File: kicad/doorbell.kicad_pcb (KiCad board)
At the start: 4 copper layers, 64 x 59 mm, 77 parts, among them J1 USB-C (USB4105), J2 WF26 bus, K1 GAQW212GS, K2 GAQY212GS, K3 GAQY412EH, K4 GAQY412EH, K5 G6K-2F-Y DC12, Q3 2N7002DW-7-F, SW1 BOOT, SW2 EN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

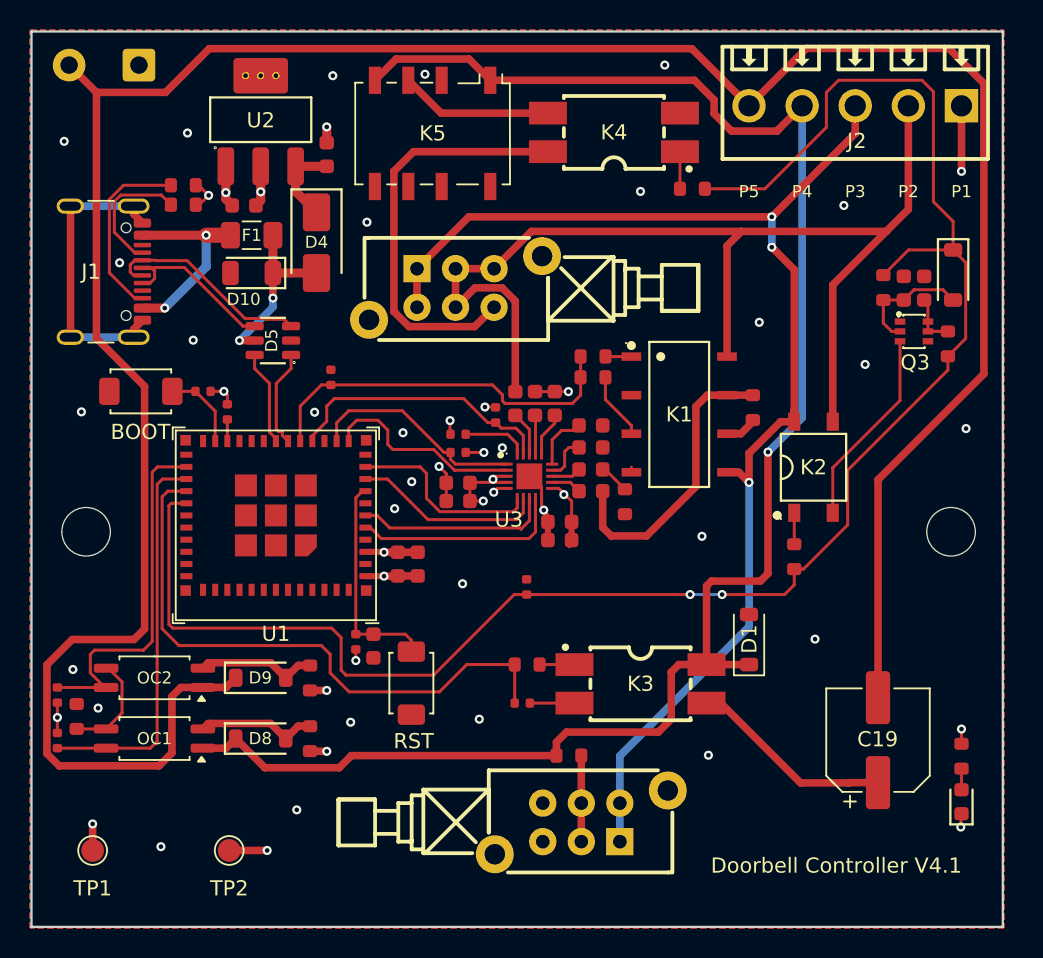
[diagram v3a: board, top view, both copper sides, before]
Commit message: Bus ESD protection placed; sim bidirectional-TVS model + coverage gate
Schematic / PCB:
- Place 4x H24VND3BA bidirectional TVS (D2/D3/D7/D12) clamping P2-P5 -> P1
- Gong cap C19 -> non-polar anti-series pair (C19+C21, 2x 47uF/50V);
  part C3349 (Honor Elec, Economy-PCBA eligible); board re-routed, DRC clean
- R29 -> PCM_JLCPCB-Resistors symbol (was generic Device:R)
- Keep the hard P1<->GND merge; 0R (C17888) / 1M (C17927) breakable bond
  documented as the respin-free alternative

sim:
- Model bidirectional TVS as anti-series Zeners with a standoff (vbr) so it is
  open across the bus range -- fixes the bus being pinned to ~0.8 V
- Add model-coverage gate: every active part must match an explicit reviewed
  model, failing loudly instead of silently using a heuristic fallback

build.sh: pinpoint route.py unrouted connections via the DRC report

docs: TODO / DESIGN / sim README brought in sync with the above
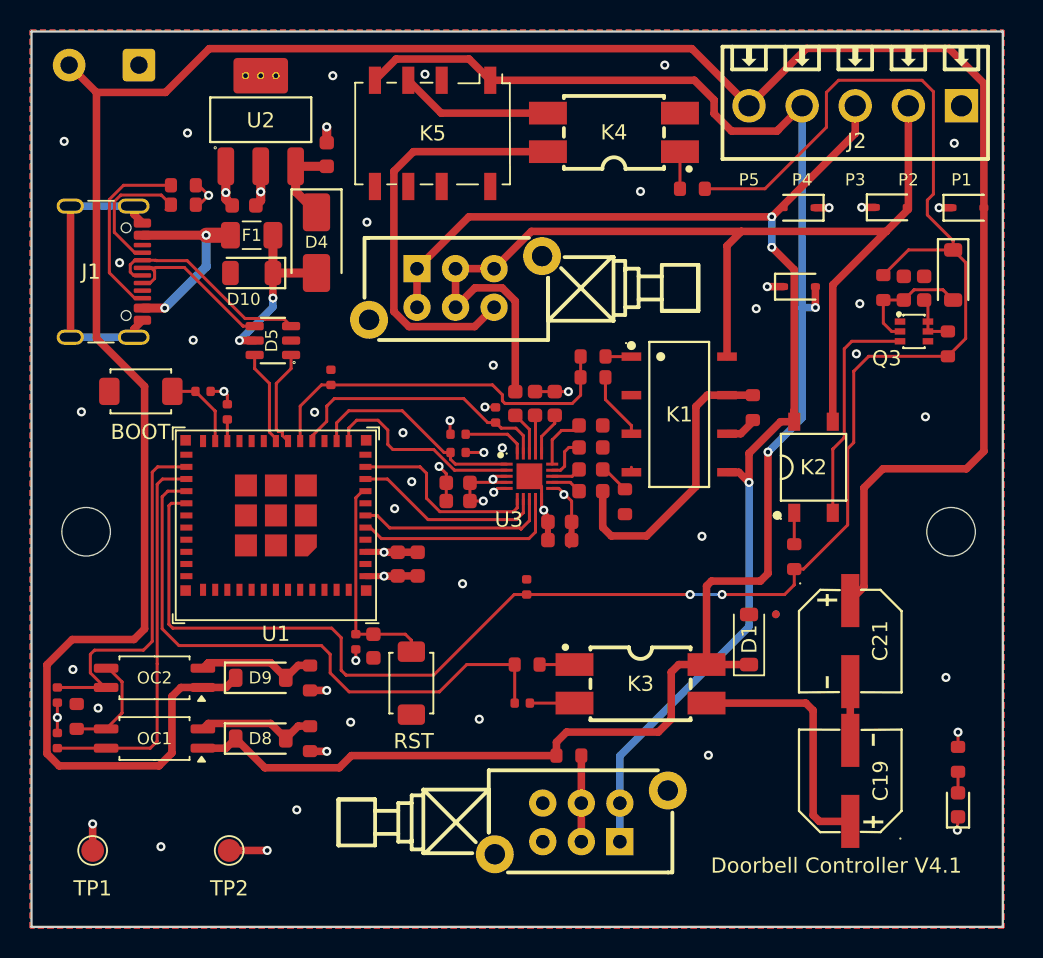
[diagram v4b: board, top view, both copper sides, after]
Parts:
- added C21: 27uF/50V, rvt1h470m0607:CAP-SMD_BD6.3-L6.6-W6.6-LS7.6-FD, F.Cu at (70.4, 56.5)
- added D12: H24VND3BA, PCM_JLCPCB:D_SOD-323, F.Cu at (78.2, 27.9)
- added D2: H24VND3BA, PCM_JLCPCB:D_SOD-323, F.Cu at (73.1, 27.9)
- added D3: H24VND3BA, PCM_JLCPCB:D_SOD-323, F.Cu at (67.0, 27.9)
- added D7: H24VND3BA, PCM_JLCPCB:D_SOD-323, F.Cu at (67.1, 33.1)
- C19: value 22uF/50V -> 27uF/50V; footprint Capacitor_SMD:CP_Elec_6.3x5.4 -> rvt1h470m0607:CAP-SMD_BD6.3-L6.6-W6.6-LS7.6-FD
- moved C19 3.25 mm to (70.4, 65.7)
- moved D6 0.31 mm to (77.5, 67.2)
- moved R15 0.31 mm to (77.5, 64.2)
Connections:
- C19 pad 2: /P5 -> /CHIME_MID
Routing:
- net /CHIME_MID: track 0.00 -> 3.87 mm
- net /DOOR_DRV: track 118.7 -> 122.1 mm
- net /CHIME_C1: track 13.5 -> 16.7 mm
- net /P5: track 177.0 -> 174.5 mm
- net /P4: track 115.6 -> 117.8 mm, vias 1 -> 2
- net /K2_CATH: track 13.2 -> 15.0 mm
- net GND: track 52.2 -> 52.8 mm, vias 43 -> 48

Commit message: Add JLCPCB tooling holes (H3–H5) + STEP fit-test export
- H3–H5: 1.152 mm NPTH JLCPCB tooling holes (PCM_JLCPCB footprint),
  asymmetric. Marked exclude-from-BOM (in_bom no) + exclude_from_pos_files/
  bom on the footprints, like H1/H2, so the BOM/CPL don't demand an LCSC #.
- DRC: exclude the footprint keepout's self-pad false positives (plus the
  attendant silk-over-copper and the floating-thieving isolated-copper
  warnings) → 0 active violations.
- build.sh: new `step` target (also run by all-route) exports
  kicad/fab/doorbell.step. Footprints carrying a truthy custom field
  STEP_Exclude are dropped via kicad/step_exclude.py (kicad-cli's
  --component-filter is include-only, so it emits the complement); SW3/SW4
  flagged so the bare board can be fit-tested against the real switches.
- DESIGN.md: document the tooling holes and the STEP / STEP_Exclude convention.
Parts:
- added H3: ~, PCM_JLCPCB:Hole_Tooling_JLCPCB, F.Cu at (24.8, 72.3)
- added H4: ~, PCM_JLCPCB:Hole_Tooling_JLCPCB, F.Cu at (23.1, 24.1)
- added H5: ~, PCM_JLCPCB:Hole_Tooling_JLCPCB, F.Cu at (78.2, 56.9)
- added Q4: 2N7002, Package_TO_SOT_SMD:SOT-23, F.Cu at (72.2, 36.9)
- C19, C21: value 27uF/50V -> 47uF/50V
- Q3: value 2N7002DW-7-F -> 2N7002; footprint mosfet_2n7002dw:SOT-363_L2.0-W1.3-P0.65-LS2.1-TL -> Package_TO_SOT_SMD:SOT-23
- moved Q3 5.53 mm to (72.1, 41.0), turned to -90 degrees
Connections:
- Q3 pad 1: GND -> /DELAY_GATE
- Q3 pad 2: /WD_GATE -> GND
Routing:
- net /K2_CATH: track 15.0 -> 7.28 mm
- net /DELAY_GATE: track 3.49 -> 10.2 mm
- net /DOOR_DRV: track 122.1 -> 121.4 mm
- net /WD_GATE: track 8.01 -> 7.40 mm
- net GND: vias 48 -> 46

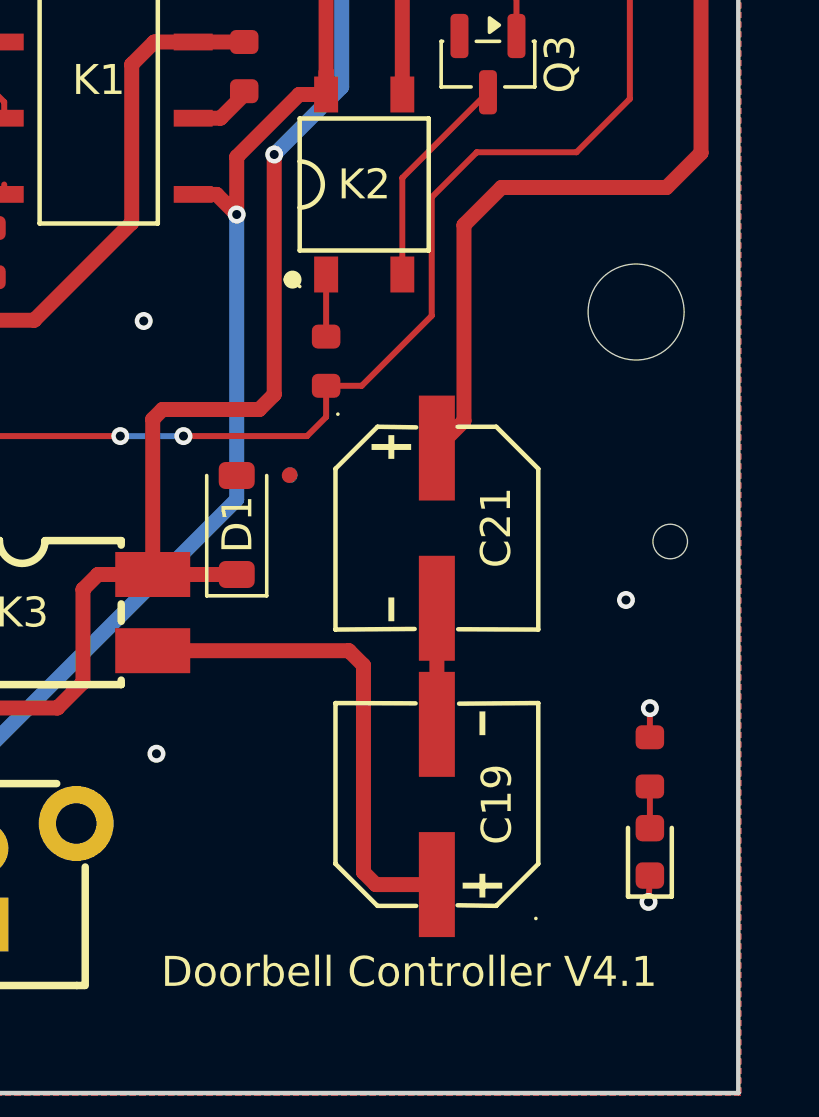
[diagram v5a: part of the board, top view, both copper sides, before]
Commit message: Fix audio/door net descriptions; correct J2 keying note; add fit-test step
Schematic Description fields (kicad/doorbell.kicad_sch):
- C18, D11: were verbatim copy-pastes of C14/D8; corrected to the
  door-lead make-delay cap (R17·C18) and door-watchdog re-arm diode
  (R25·C20·D11) they actually are, per the netlist.
- C14, R28, K1: dropped the stale "K1 gates ->P4" claim — K1 switches
  P2/P3 (the talk handshake via R28), never P4.

Docs:
- TODO/DESIGN/REQUIREMENTS: J2 is a fixed screw terminal (DB125-3.5-5P,
  no plug) — keying is N/A; SAFE-2 survive-miswire rests on the
  bidirectional front-end + non-polar C19 + silkscreen labels.
- ORDERING: added a pre-fab 3D-print fit-test gate (board/enclosure
  fit, connector access, SW3/SW4 actuation — MECH-1/1a).

Verified with ./build.sh all-route: ERC/DRC clean, sim 46/46, fab + STEP
re-exported. Zone fills refreshed on save.
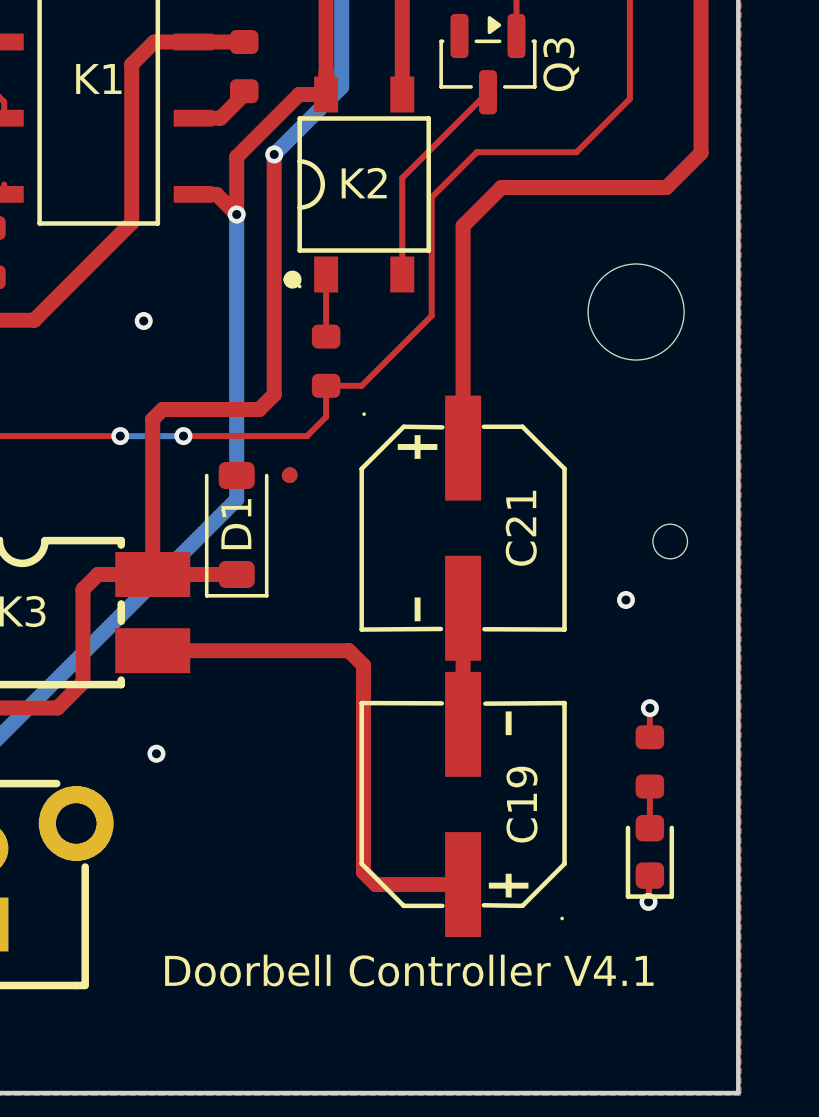
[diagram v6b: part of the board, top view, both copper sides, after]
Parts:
- moved C19 0.88 mm to (71.3, 65.7)
- moved C21 0.88 mm to (71.3, 56.5)
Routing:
- net /CHIME_C1: track 16.7 -> 17.6 mm
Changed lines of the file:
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@@
 		(layer "F.Cu")
 		(at 52.7 68.4)
-		(property "STEP_Exclude" "true"
-			(at 0 0 0)
-			(unlocked yes)
-			(layer "F.Fab")
-			(hide yes)
-			(effects
-				(font
-					(size 1 1)
-					(thickness 0.15)
-				)
-			)
-		)
 		(property "Reference" "SW4"
 			(at 0.05 4.51 0)
@@
 			)
 		)
+		(property "STEP_Exclude" "true"
+			(at 0 0 0)
+			(unlocked yes)
+			(layer "F.Fab")
+			(hide yes)
+			(effects
+				(font
+					(size 1 1)
+					(thickness 0.15)
+				)
+			)
+		)
 		(property "LCSC Part" "C398940"
 			(at 0 0 0)
@@
 	(footprint "rvt1h470m0607:CAP-SMD_BD6.3-L6.6-W6.6-LS7.6-FD"
 		(layer "F.Cu")
-		(at 70.421786 65.665474 90)
+		(at 71.296786 65.665474 90)
 		(descr "47uF 50V ±20%")
 		(property "Reference" "C19"
@@
 		(layer "F.Cu")
 		(at 44.4125 33.185 180)
-		(property "STEP_Exclude" "true"
-			(at 0 0 0)
-			(unlocked yes)
-			(layer "F.Fab")
-			(hide yes)
-			(effects
-				(font
-					(size 1 1)
-					(thickness 0.15)
-				)
-			)
-		)
 		(property "Reference" "SW3"
 			(at -0.0275 -4.765 0)
@@
 			)
 		)
+		(property "STEP_Exclude" "true"
+			(at 0 0 0)
+			(unlocked yes)
+			(layer "F.Fab")
+			(hide yes)
+			(effects
+				(font
+					(size 1 1)
+					(thickness 0.15)
+				)
+			)
+		)
 		(property "LCSC Part" "C398940"
 			(at 0 0 0)
@@
 	(footprint "rvt1h470m0607:CAP-SMD_BD6.3-L6.6-W6.6-LS7.6-FD"
 		(layer "F.Cu")
-		(at 70.421786 56.455474 -90)
+		(at 71.296786 56.455474 -90)
 		(descr "47uF 50V ±20%")
 		(property "Reference" "C21"
@@
 	)
 	(segment
+		(start 79.227 19.708)
+		(end 79.227 43.948)
+		(width 0.5)
+		(layer "F.Cu")
+		(net "/P5")
+	)
+	(segment
 		(start 17.488 58.012)
 		(end 19.15 56.35)
@@
 	)
 	(segment
-		(start 71.325 46.35)
-		(end 71.325 52.88226)
+		(start 67.535 17.4)
+		(end 76.919 17.4)
 		(width 0.5)
 		(layer "F.Cu")
@@
 	)
 	(segment
-		(start 76.919 17.4)
-		(end 79.227 19.708)
+		(start 78.075 45.1)
+		(end 72.575 45.1)
 		(width 0.5)
 		(layer "F.Cu")
@@
 	)
 	(segment
-		(start 67.535 17.4)
-		(end 76.919 17.4)
-		(width 0.5)
-		(layer "F.Cu")
-		(net "/P5")
-	)
-	(segment
 		(start 19.15 56.35)
 		(end 23.225 56.35)
@@
 	)
 	(segment
-		(start 20.75 20.3)
-		(end 25.3 20.3)
-		(width 0.5)
-		(layer "F.Cu")
-		(net "/P5")
-	)
-	(segment
-		(start 27.7625 59.51)
-		(end 26.315 59.51)
-		(width 0.5)
-		(layer "F.Cu")
-		(net "/P5")
-	)
-	(segment
-		(start 78.075 45.1)
-		(end 72.575 45.1)
+		(start 63.75 21.185)
+		(end 67.535 17.4)
 		(width 0.5)
 		(layer "F.Cu")
@@
 	)
 	(segment
-		(start 29.290001 59.51)
-		(end 27.7625 59.51)
+		(start 72.575 45.1)
+		(end 71.296786 46.378214)
 		(width 0.5)
 		(layer "F.Cu")
@@
 	)
 	(segment
-		(start 71.325 52.88226)
-		(end 70.421786 53.785474)
+		(start 20.75 20.3)
+		(end 25.3 20.3)
 		(width 0.5)
 		(layer "F.Cu")
@@
 	)
 	(segment
-		(start 72.575 45.1)
-		(end 71.325 46.35)
+		(start 27.7625 59.51)
+		(end 26.315 59.51)
 		(width 0.5)
 		(layer "F.Cu")
@@
 	)
 	(segment
-		(start 63.75 21.185)
-		(end 67.535 17.4)
+		(start 29.290001 59.51)
+		(end 27.7625 59.51)
 		(width 0.5)
 		(layer "F.Cu")
@@
 	)
 	(segment
-		(start 79.227 19.708)
-		(end 79.227 43.948)
+		(start 63.75 21.185)
+		(end 59.981803 17.416803)
 		(width 0.5)
 		(layer "F.Cu")
@@
 	)
 	(segment
-		(start 63.75 21.185)
-		(end 59.981803 17.416803)
+		(start 76.919 17.4)
+		(end 79.227 19.708)
 		(width 0.5)
 		(layer "F.Cu")
@@
 	)
 	(segment
+		(start 71.296786 46.378214)
+		(end 71.296786 53.785474)
+		(width 0.5)
+		(layer "F.Cu")
+		(net "/P5")
+	)
+	(segment
 		(start 25.725 60.1)
 		(end 25.725 63.825)
@@
 	)
 	(segment
-		(start 60.95 60.54)
-		(end 67.49 60.54)
+		(start 67.49 60.54)
+		(end 67.975 61.025)
 		(width 0.5)
 		(layer "F.Cu")
@@
 	)
 	(segment
-		(start 67.975 61.025)
-		(end 67.975 67.925)
+		(start 67.975 67.925)
+		(end 68.385474 68.335474)
 		(width 0.5)
 		(layer "F.Cu")
@@
 	)
 	(segment
-		(start 67.49 60.54)
-		(end 67.975 61.025)
+		(start 67.975 61.025)
+		(end 67.975 67.925)
 		(width 0.5)
 		(layer "F.Cu")
@@
 	)
 	(segment
-		(start 68.385474 68.335474)
-		(end 70.421786 68.335474)
+		(start 60.95 60.54)
+		(end 67.49 60.54)
 		(width 0.5)
 		(layer "F.Cu")
@@
 	)
 	(segment
-		(start 67.975 67.925)
-		(end 68.385474 68.335474)
+		(start 68.385474 68.335474)
+		(end 71.296786 68.335474)
 		(width 0.5)
 		(layer "F.Cu")
@@
 	)
 	(segment
-		(start 70.421786 62.995474)
-		(end 70.421786 59.125474)
+		(start 71.296786 62.995474)
+		(end 71.296786 59.125474)
 		(width 0.5)
 		(layer "F.Cu")

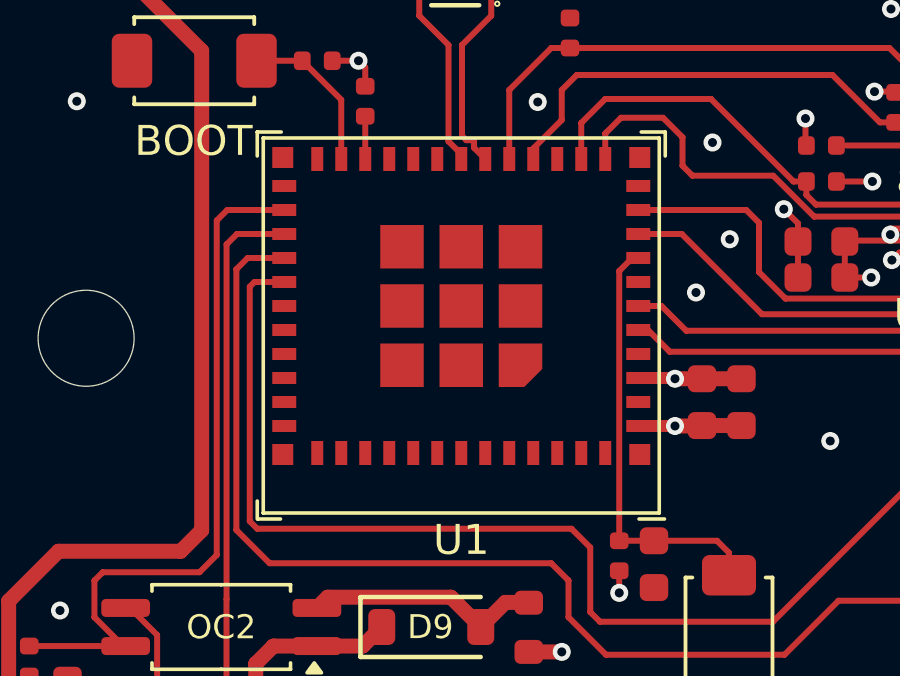
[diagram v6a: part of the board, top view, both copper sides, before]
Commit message: Add GND stitching via ring around U1 (ESP32-C6-MINI-1U) EPAD
Ties the module's central GND/thermal EPAD and perimeter GND pins down to
the In2 GND plane with a ring of vias placed in the clear band between the
outer pins and the EPAD — on GND pour, none in a pad, so the no-via-in-pad
rule holds (no wicking, no POFV needed). The EPAD's own 0.525 mm inter-pad
gaps are too tight for a clearance-legal via, so stitching goes around it,
not through it.

Kept sparse and trace-aware: In1 is the +3V3 plane, so vias are spread
(not a dense wall) to avoid Swiss-cheesing it, and routed clear of the
signal escapes (e.g. the /EN trace). Positions hand-finalized.

Verified: DRC 0 violations / 0 unconnected, board fully routed.
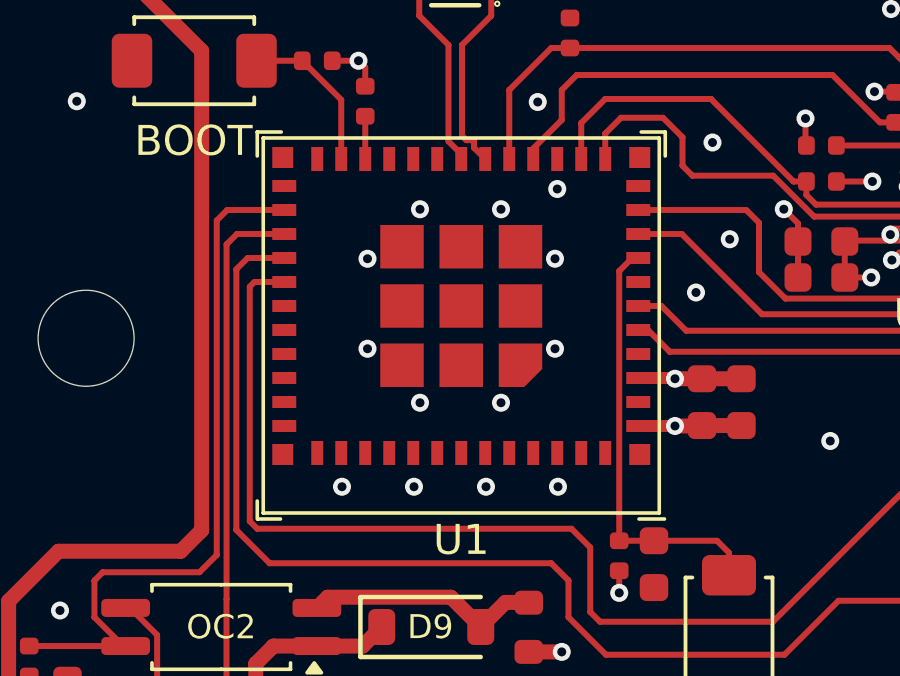
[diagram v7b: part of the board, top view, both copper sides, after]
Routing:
- net GND: vias 46 -> 59
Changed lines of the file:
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@@
+	)
+	(via
+		(at 31.2 44.95)
+		(size 0.6)
+		(drill 0.3)
+		(layers "F.Cu" "B.Cu")
+		(free yes)
+		(net "GND")
 	)
 	(via
@@
 	)
 	(via
+		(at 29.45 46.6)
+		(size 0.6)
+		(drill 0.3)
+		(layers "F.Cu" "B.Cu")
+		(free yes)
+		(net "GND")
+	)
+	(via
 		(at 77.275 23.65)
 		(size 0.6)
@@
 	)
 	(via
+		(at 33.4 54.2)
+		(size 0.6)
+		(drill 0.3)
+		(layers "F.Cu" "B.Cu")
+		(free yes)
+		(net "GND")
+	)
+	(via
 		(at 40.4 47.725)
 		(size 0.6)
@@
 	)
 	(via
+		(at 29.45 49.6)
+		(size 0.6)
+		(drill 0.3)
+		(layers "F.Cu" "B.Cu")
+		(free yes)
+		(net "GND")
+	)
+	(via
 		(at 64.95 33.1)
 		(size 0.6)
@@
 	)
 	(via
+		(at 35.7 46.6)
+		(size 0.6)
+		(drill 0.3)
+		(layers "F.Cu" "B.Cu")
+		(free yes)
+		(net "GND")
+	)
+	(via
 		(at 39.7 52.175)
 		(size 0.6)
@@
 	)
 	(via
+		(at 35.7 49.6)
+		(size 0.6)
+		(drill 0.3)
+		(layers "F.Cu" "B.Cu")
+		(free yes)
+		(net "GND")
+	)
+	(via
 		(at 60.65 49.55)
 		(size 0.6)
@@
 	)
 	(via
+		(at 35.775 44.275)
+		(size 0.6)
+		(drill 0.3)
+		(layers "F.Cu" "B.Cu")
+		(free yes)
+		(net "GND")
+	)
+	(via
+		(at 28.6 54.2)
+		(size 0.6)
+		(drill 0.3)
+		(layers "F.Cu" "B.Cu")
+		(free yes)
+		(net "GND")
+	)
+	(via
 		(at 77.4775 68.9145)
 		(size 0.6)
@@
 	)
 	(via
+		(at 35.8 54.2)
+		(size 0.6)
+		(drill 0.3)
+		(layers "F.Cu" "B.Cu")
+		(free yes)
+		(net "GND")
+	)
+	(via
+		(at 31 54.2)
+		(size 0.6)
+		(drill 0.3)
+		(layers "F.Cu" "B.Cu")
+		(free yes)
+		(net "GND")
+	)
+	(via
 		(at 51.849999 40.015001)
 		(size 0.6)
@@
 	)
 	(via
+		(at 31.2 51.4)
+		(size 0.6)
+		(drill 0.3)
+		(layers "F.Cu" "B.Cu")
+		(free yes)
+		(net "GND")
+	)
+	(via
 		(at 18.625 23.525)
 		(size 0.6)
@@
 	)
 	(via
+		(at 33.9 51.4)
+		(size 0.6)
+		(drill 0.3)
+		(layers "F.Cu" "B.Cu")
+		(free yes)
+		(net "GND")
+	)
+	(via
 		(at 20.5 68.5)
 		(size 0.6)
 		(drill 0.3)
+		(layers "F.Cu" "B.Cu")
+		(free yes)
+		(net "GND")
+	)
+	(via
+		(at 33.9 44.95)
+		(size 0.6)
+		(drill 0.3)
